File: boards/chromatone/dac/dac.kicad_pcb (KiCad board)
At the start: 2 copper layers, 56 x 36 mm, 31 parts, among them J1 Pi I2S, J2 Line out, U1 PCM5102A, U2 ME6211C33

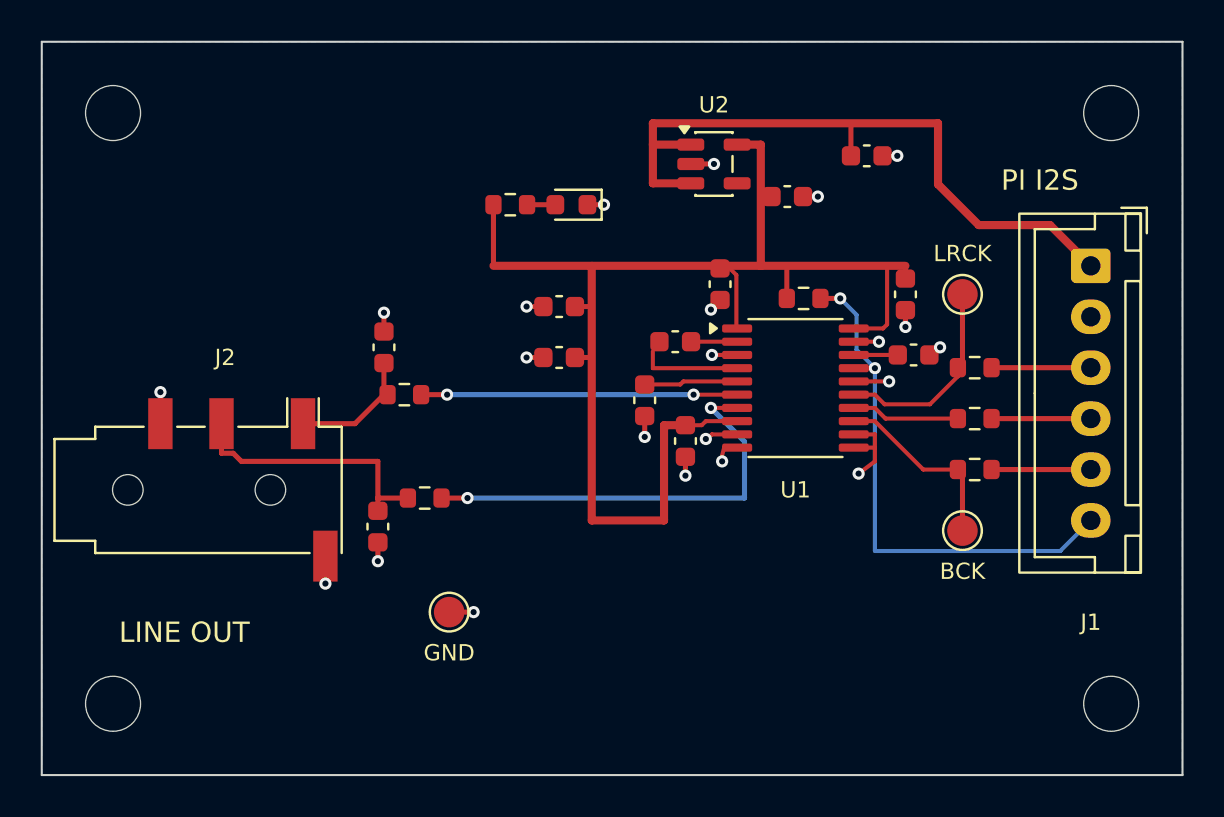
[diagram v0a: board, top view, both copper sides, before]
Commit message: chromatone/dac: review fixes (audio/XSMT routing off the ground returns, decoupling at pins, full JLCPCB BOM)
Co-Authored-By: Claude Fable 5.1 <noreply@anthropic.com>
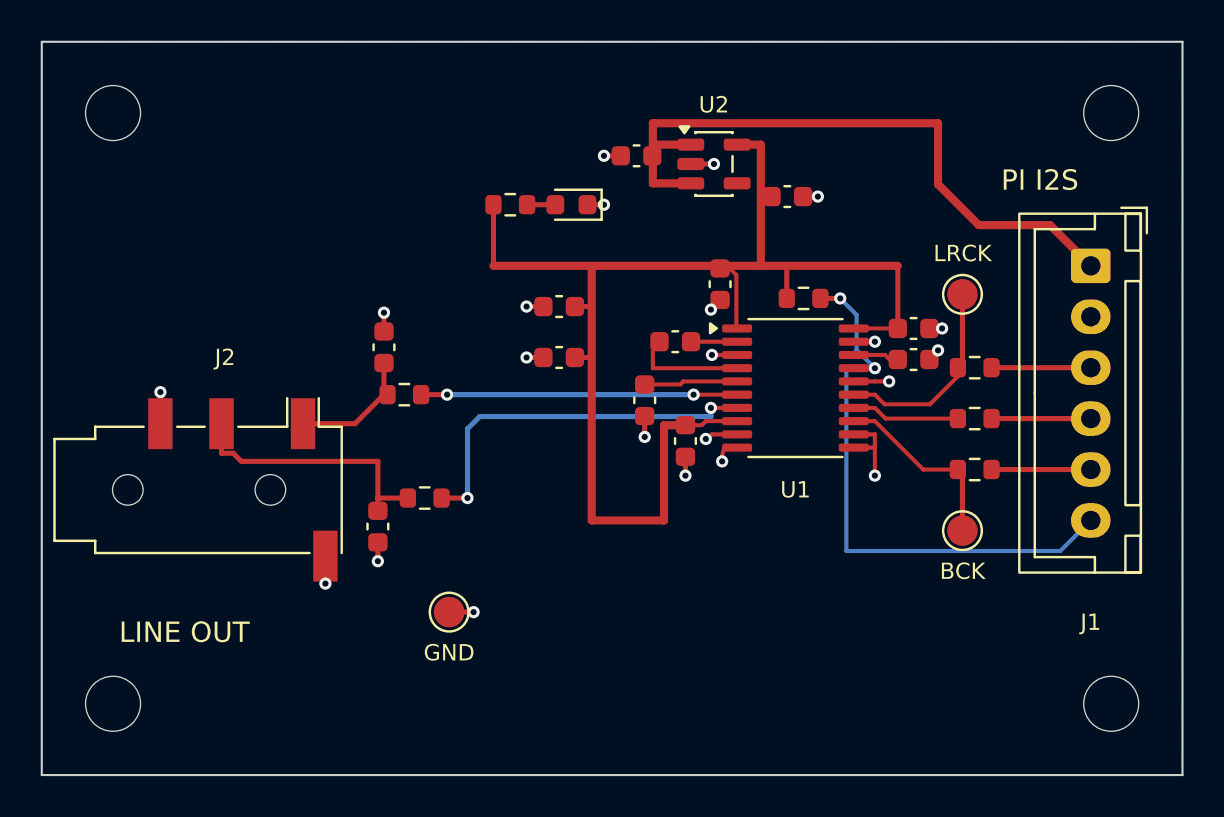
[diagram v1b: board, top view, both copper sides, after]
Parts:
- moved C1 11.3 mm to (79.2, 55.6), turned to 180 degrees
- moved C11 1.72 mm to (92.8, 64.1), turned to 0 degrees
- moved C7 0.22 mm to (92.8, 65.6)
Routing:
- net Net-(J1-Pin_6): track 26.3 -> 29.1 mm
- net Net-(U1-OUTR): track 21.3 -> 18.6 mm
- net +5V: track 34.4 -> 32.9 mm
- net GND: track 26.3 -> 25.7 mm
